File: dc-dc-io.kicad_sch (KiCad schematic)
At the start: 41 parts, among them U20 MPM54304GMN, U28 PAC1944T-E

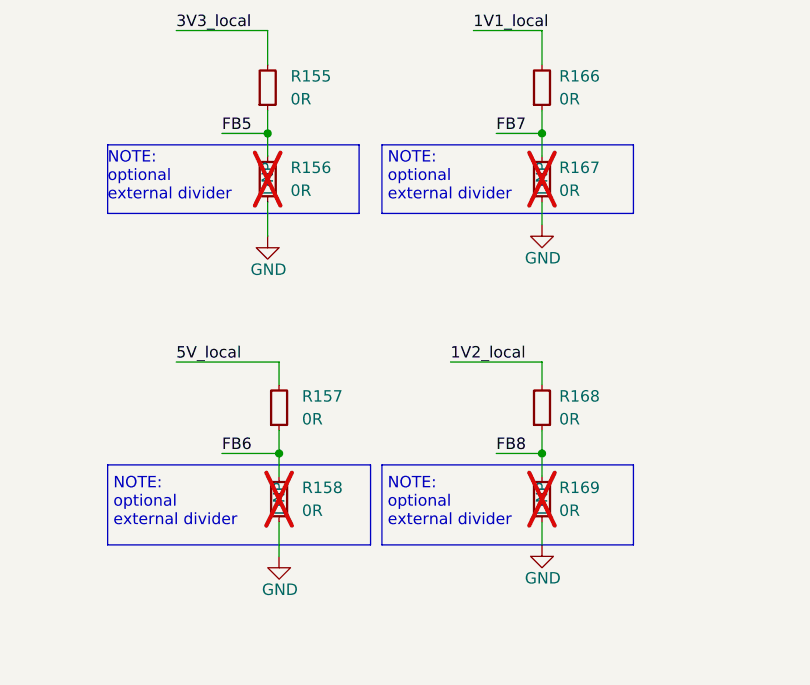
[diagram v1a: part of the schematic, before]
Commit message: [#69629] Fix DNP attributes
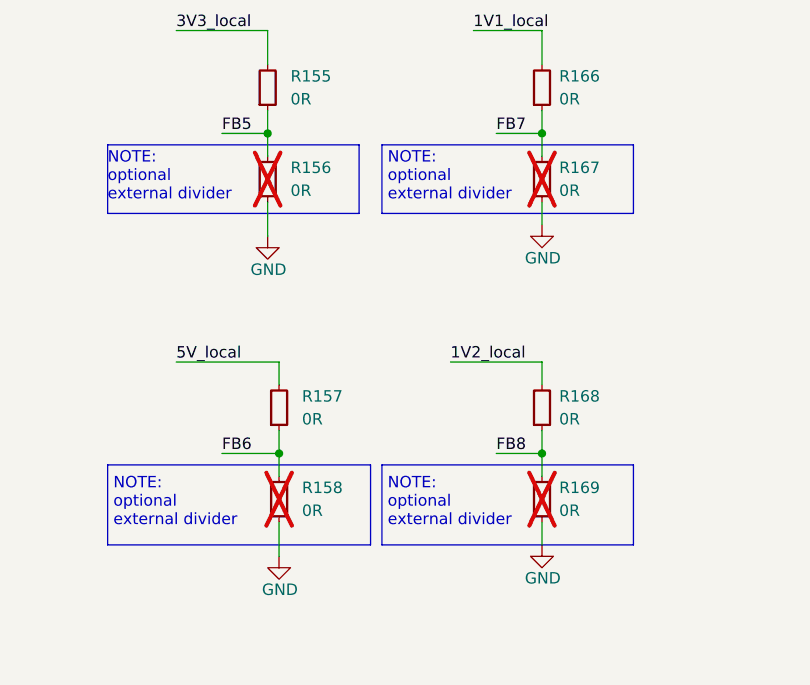
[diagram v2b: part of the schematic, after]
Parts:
- R156, R158, R167, R169: DNP DNP -> (none)

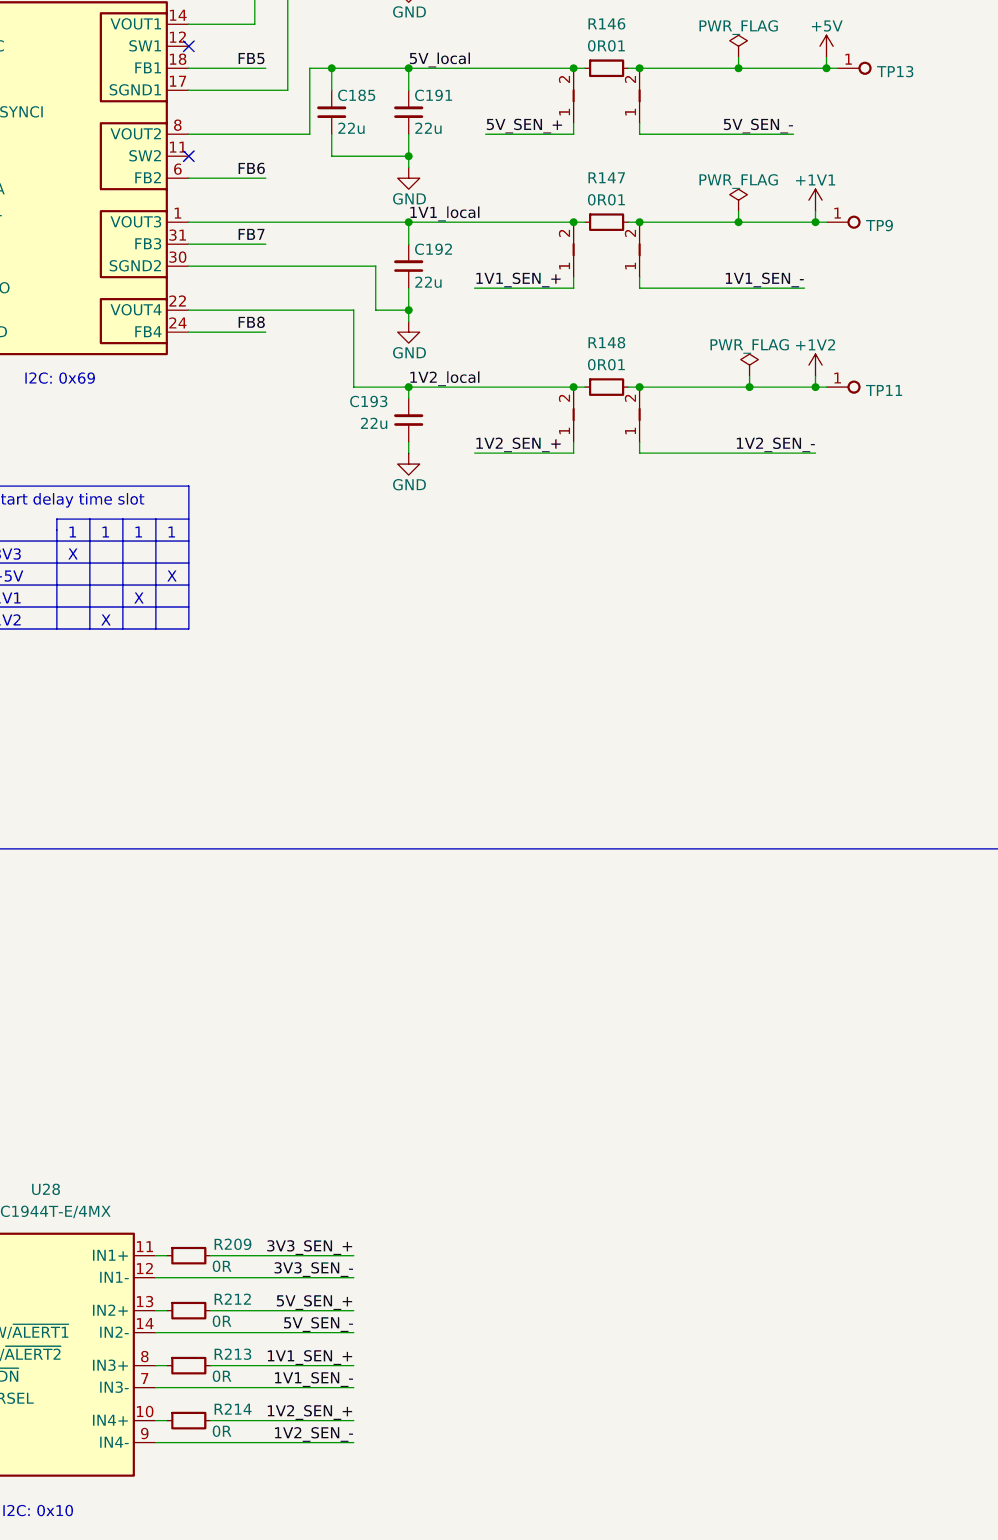
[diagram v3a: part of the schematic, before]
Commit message: [#70235] Improve power supply labels
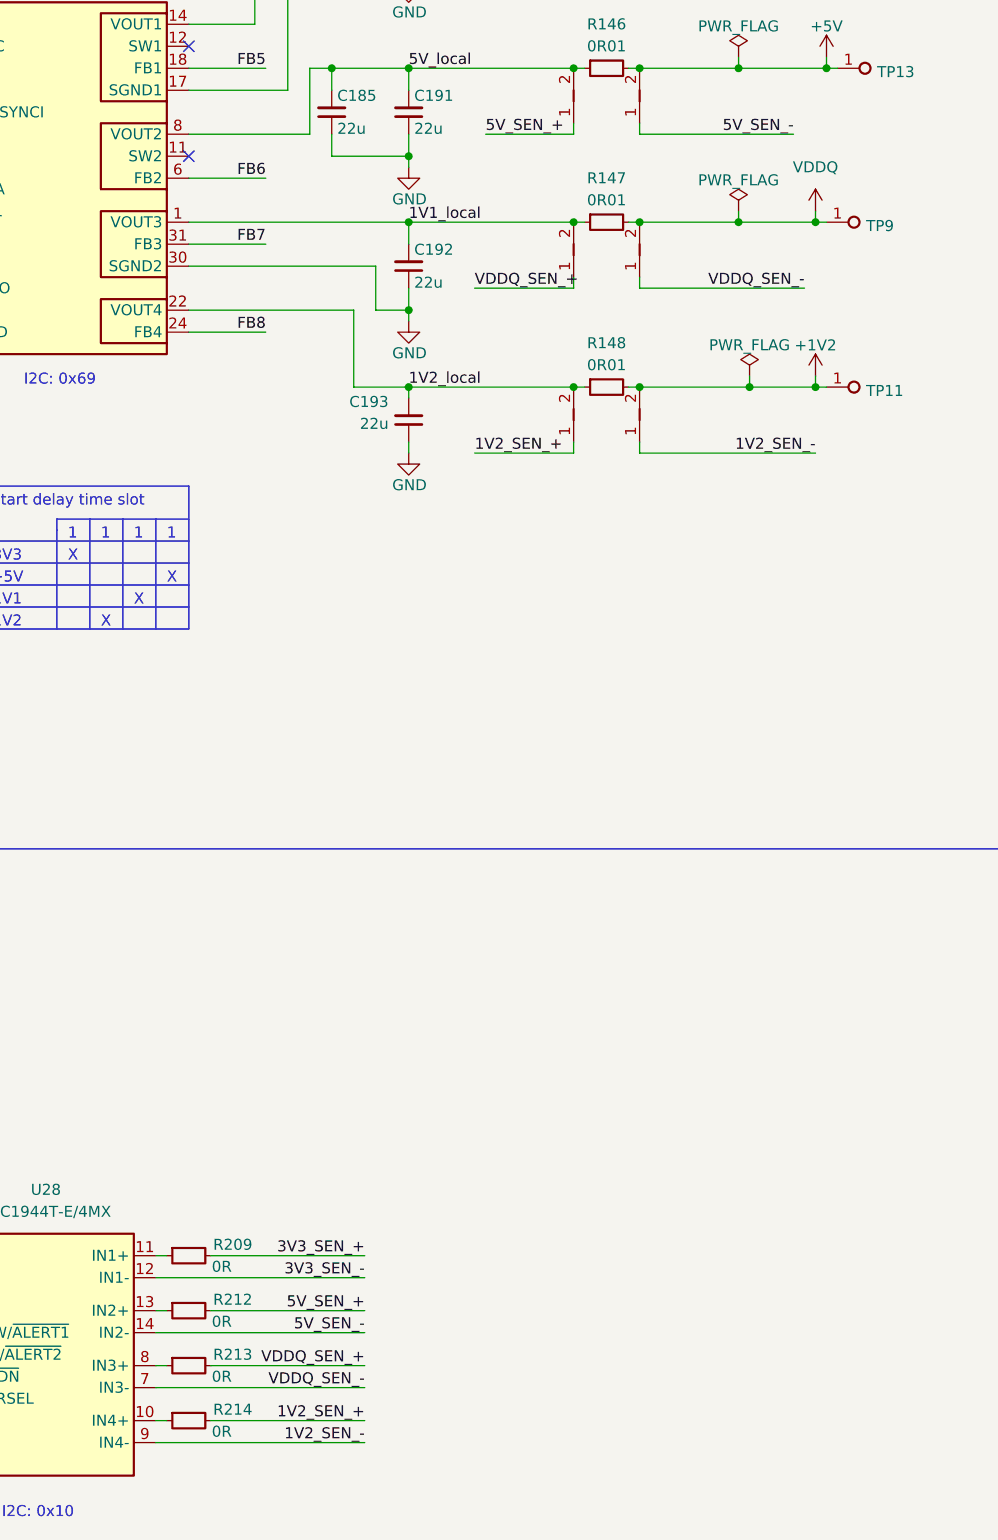
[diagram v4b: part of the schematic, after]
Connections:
- net +1V1 renamed VDDQ
- net 1V1_SEN_+ renamed VDDQ_SEN_+
- net 1V1_SEN_- renamed VDDQ_SEN_-
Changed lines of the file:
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@@
 	(wire
 		(pts
+			(xy 173.99 226.06) (xy 198.12 226.06)
+		)
+		(stroke
+			(width 0)
+			(type default)
+		)
+	)
+	(wire
+		(pts
 			(xy 222.25 59.69) (xy 210.82 59.69)
 		)
@@
 	(wire
 		(pts
+			(xy 180.34 217.17) (xy 198.12 217.17)
+		)
+		(stroke
+			(width 0)
+			(type default)
+		)
+	)
+	(wire
+		(pts
 			(xy 203.2 62.23) (xy 203.2 63.5)
 		)
@@
 	(wire
 		(pts
-			(xy 128.27 58.42) (xy 128.27 59.69)
+			(xy 180.34 210.82) (xy 198.12 210.82)
 		)
 		(stroke
@@
 	(wire
 		(pts
-			(xy 194.31 59.69) (xy 194.31 62.23)
+			(xy 128.27 58.42) (xy 128.27 59.69)
 		)
 		(stroke
@@
 	(wire
 		(pts
-			(xy 173.99 217.17) (xy 175.26 217.17)
+			(xy 194.31 59.69) (xy 194.31 62.23)
 		)
 		(stroke
@@
 	(wire
 		(pts
-			(xy 242.57 110.49) (xy 250.19 110.49)
+			(xy 173.99 217.17) (xy 175.26 217.17)
 		)
 		(stroke
@@
 	(wire
 		(pts
-			(xy 242.57 109.22) (xy 242.57 110.49)
+			(xy 242.57 110.49) (xy 250.19 110.49)
 		)
 		(stroke
@@
 	(wire
 		(pts
-			(xy 241.3 73.66) (xy 251.46 73.66)
+			(xy 242.57 109.22) (xy 242.57 110.49)
 		)
 		(stroke
@@
 	(wire
 		(pts
-			(xy 229.87 91.44) (xy 241.3 91.44)
+			(xy 241.3 73.66) (xy 251.46 73.66)
 		)
 		(stroke
@@
 	(wire
 		(pts
-			(xy 173.99 219.71) (xy 196.85 219.71)
+			(xy 229.87 91.44) (xy 241.3 91.44)
 		)
 		(stroke
@@
 	(wire
 		(pts
+			(xy 173.99 213.36) (xy 198.12 213.36)
+		)
+		(stroke
+			(width 0)
+			(type default)
+		)
+	)
+	(wire
+		(pts
 			(xy 339.09 104.14) (xy 339.09 106.68)
 		)
@@
 		)
 	)
-	(wire
-		(pts
-			(xy 173.99 226.06) (xy 196.85 226.06)
-		)
-		(stroke
-			(width 0)
-			(type default)
-		)
-	)
 	(polyline
 		(pts
@@
 		)
 	)
-	(wire
-		(pts
-			(xy 173.99 232.41) (xy 196.85 232.41)
-		)
-		(stroke
-			(width 0)
-			(type default)
-		)
-	)
 	(polyline
 		(pts
@@
 	(wire
 		(pts
-			(xy 180.34 223.52) (xy 196.85 223.52)
+			(xy 147.32 231.14) (xy 147.32 233.68)
 		)
 		(stroke
@@
 	(wire
 		(pts
-			(xy 147.32 231.14) (xy 147.32 233.68)
+			(xy 128.27 71.12) (xy 128.27 73.66)
 		)
 		(stroke
@@
 	(wire
 		(pts
-			(xy 128.27 71.12) (xy 128.27 73.66)
+			(xy 189.23 62.23) (xy 194.31 62.23)
 		)
 		(stroke
@@
 	(wire
 		(pts
-			(xy 189.23 62.23) (xy 194.31 62.23)
+			(xy 173.99 232.41) (xy 198.12 232.41)
 		)
 		(stroke
@@
 	(wire
 		(pts
-			(xy 180.34 210.82) (xy 196.85 210.82)
-		)
-		(stroke
-			(width 0)
-			(type default)
-		)
-	)
-	(wire
-		(pts
 			(xy 196.85 110.49) (xy 203.2 110.49)
 		)
@@
 	(wire
 		(pts
-			(xy 180.34 217.17) (xy 196.85 217.17)
-		)
-		(stroke
-			(width 0)
-			(type default)
-		)
-	)
-	(wire
-		(pts
 			(xy 203.2 110.49) (xy 203.2 111.76)
 		)
@@
 	(wire
 		(pts
-			(xy 241.3 50.8) (xy 241.3 52.07)
+			(xy 173.99 219.71) (xy 198.12 219.71)
 		)
 		(stroke
@@
 	(wire
 		(pts
-			(xy 173.99 213.36) (xy 196.85 213.36)
+			(xy 241.3 50.8) (xy 241.3 52.07)
 		)
 		(stroke
@@
 	(wire
 		(pts
-			(xy 180.34 229.87) (xy 196.85 229.87)
+			(xy 128.27 71.12) (xy 149.86 71.12)
 		)
 		(stroke
@@
 	(wire
 		(pts
-			(xy 128.27 71.12) (xy 149.86 71.12)
+			(xy 250.19 109.22) (xy 250.19 110.49)
 		)
 		(stroke
@@
 	(wire
 		(pts
-			(xy 250.19 109.22) (xy 250.19 110.49)
+			(xy 177.8 101.6) (xy 196.85 101.6)
 		)
 		(stroke
@@
 	(wire
 		(pts
-			(xy 177.8 101.6) (xy 196.85 101.6)
+			(xy 222.25 52.07) (xy 223.52 52.07)
 		)
 		(stroke
@@
 	(wire
 		(pts
-			(xy 222.25 52.07) (xy 223.52 52.07)
+			(xy 180.34 223.52) (xy 198.12 223.52)
 		)
 		(stroke
@@
 		)
 	)
+	(wire
+		(pts
+			(xy 180.34 229.87) (xy 198.12 229.87)
+		)
+		(stroke
+			(width 0)
+			(type default)
+		)
+	)
 	(polyline
 		(pts
@@
 		)
 	)
-	(label "1V1_SEN_+"
+	(label "VDDQ_SEN_+"
 		(at 210.82 99.06 0)
 		(fields_autoplaced yes)
@@
 		)
 	)
-	(label "1V1_SEN_-"
+	(label "VDDQ_SEN_-"
 		(at 248.92 99.06 180)
 		(fields_autoplaced yes)
@@
 	)
 	(label "1V2_SEN_+"
-		(at 196.85 229.87 180)
+		(at 198.12 229.87 180)
 		(fields_autoplaced yes)
 		(effects
@@
 	)
 	(label "3V3_SEN_-"
-		(at 196.85 213.36 180)
+		(at 198.12 213.36 180)
 		(fields_autoplaced yes)
 		(effects
@@
 	)
 	(label "1V2_SEN_-"
-		(at 196.85 232.41 180)
+		(at 198.12 232.41 180)
 		(fields_autoplaced yes)
 		(effects
@@
 	)
 	(label "5V_SEN_-"
-		(at 196.85 219.71 180)
+		(at 198.12 219.71 180)
 		(fields_autoplaced yes)
 		(effects
@@
 	)
 	(label "5V_SEN_+"
-		(at 196.85 217.17 180)
+		(at 198.12 217.17 180)
 		(fields_autoplaced yes)
 		(effects
@@
 		)
 	)
-	(label "1V1_SEN_-"
-		(at 196.85 226.06 180)
+	(label "VDDQ_SEN_-"
+		(at 198.12 226.06 180)
 		(fields_autoplaced yes)
 		(effects
@@
 		)
 	)
-	(label "1V1_SEN_+"
-		(at 196.85 223.52 180)
+	(label "VDDQ_SEN_+"
+		(at 198.12 223.52 180)
 		(fields_autoplaced yes)
 		(effects
@@
 	)
 	(label "3V3_SEN_+"
-		(at 196.85 210.82 180)
+		(at 198.12 210.82 180)
 		(fields_autoplaced yes)
 		(effects
@@
 	)
 	(symbol
+		(lib_id "antmicropower:VDD")
+		(at 250.19 90.17 0)
+		(unit 1)
+		(exclude_from_sim no)
+		(in_bom yes)
+		(on_board yes)
+		(dnp no)
+		(fields_autoplaced yes)
+		(property "Reference" "#PWR048"
+			(at 250.19 93.98 0)
+			(effects
+				(font
+					(size 1.27 1.27)
+				)
+				(hide yes)
+			)
+		)
+		(property "Value" "VDDQ"
+			(at 250.19 85.09 0)
+			(effects
+				(font
+					(size 1.27 1.27)
+				)
+			)
+		)
+		(property "Footprint" ""
+			(at 250.19 90.17 0)
+			(effects
+				(font
+					(size 1.27 1.27)
+				)
+				(hide yes)
+			)
+		)
+		(property "Datasheet" ""
+			(at 250.19 90.17 0)
+			(effects
+				(font
+					(size 1.27 1.27)
+				)
+				(hide yes)
+			)
+		)
+		(property "Description" ""
+			(at 250.19 90.17 0)
+			(effects
+				(font
+					(size 1.27 1.27)
+				)
+				(hide yes)
+			)
+		)
+		(pin "1"
+		)
+		(instances
+			(project "data-center-rdimm-ddr5-tester"
+				(path "/1faa6543-e26a-4449-8bac-ee14b9f19e5f/00000000-0000-0000-0000-000060225b0c/5b621c5d-ceb0-481d-9809-c89bf3097b70"
+					(reference "#PWR048")
+					(unit 1)
+				)
+			)
+		)
+	)
+	(symbol
 		(lib_id "antmicroResistors0402:R_0R_0402")
 		(at 339.09 111.76 90)
@@
 					(unit 1)
 				)
-			)
-		)
-	)
-	(symbol
-		(lib_id "antmicropower:+1V1")
-		(at 250.19 90.17 0)
-		(unit 1)
-		(exclude_from_sim no)
-		(in_bom yes)
-		(on_board yes)
-		(dnp no)
-		(property "Reference" "#PWR0323"
-			(at 250.19 93.98 0)
-			(effects
-				(font
-					(size 1.27 1.27)
-				)
-				(hide yes)
-			)
-		)
-		(property "Value" "+1V1"
-			(at 250.19 86.614 0)
-			(effects
-				(font
-					(size 1.27 1.27)
-				)
-			)
-		)
-		(property "Footprint" ""
-			(at 250.19 90.17 0)
-			(effects
-				(font
-					(size 1.27 1.27)
-				)
-				(hide yes)
-			)
-		)
-		(property "Datasheet" ""
-			(at 250.19 90.17 0)
-			(effects
-				(font
-					(size 1.27 1.27)
-				)
-				(hide yes)
-			)
-		)
-		(property "Description" ""
-			(at 250.19 90.17 0)
-			(effects
-				(font
-					(size 1.27 1.27)
-				)
-				(hide yes)
-			)
-		)
-		(pin "1"
-		)
-		(instances
-			(project "data-center-rdimm-ddr5-tester"
-				(path "/1faa6543-e26a-4449-8bac-ee14b9f19e5f/00000000-0000-0000-0000-000060225b0c/5b621c5d-ceb0-481d-9809-c89bf3097b70"
-					(reference "#PWR0323")
-					(unit 1)
-				)
